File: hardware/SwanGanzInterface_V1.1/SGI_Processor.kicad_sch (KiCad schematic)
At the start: 29 parts, among them J2 Conn_01x08_Pin, SW2 MODE, SW3 ENTER, SW4 MODE, U4 XM0G3507QPTRQ1, U5 AdaFruit_1590, Y1 ABM8AIG-40.000MHZ-12-2Z-T3

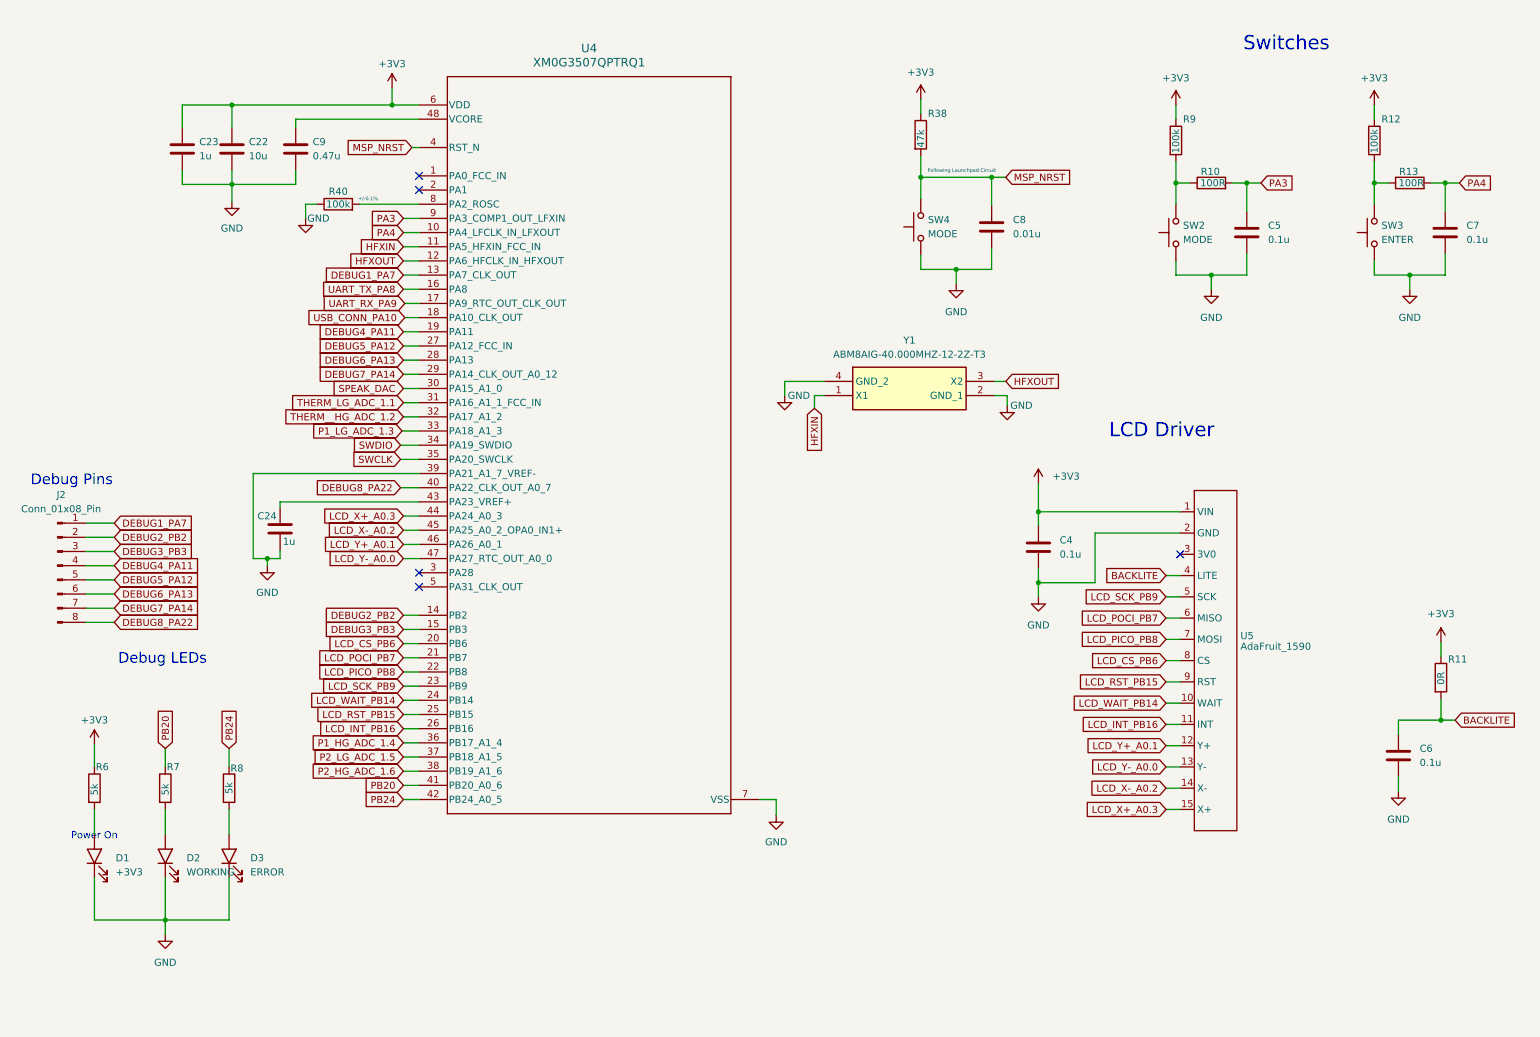
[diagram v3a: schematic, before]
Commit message: Worked on FT232R circuit - RTS, CTS etc
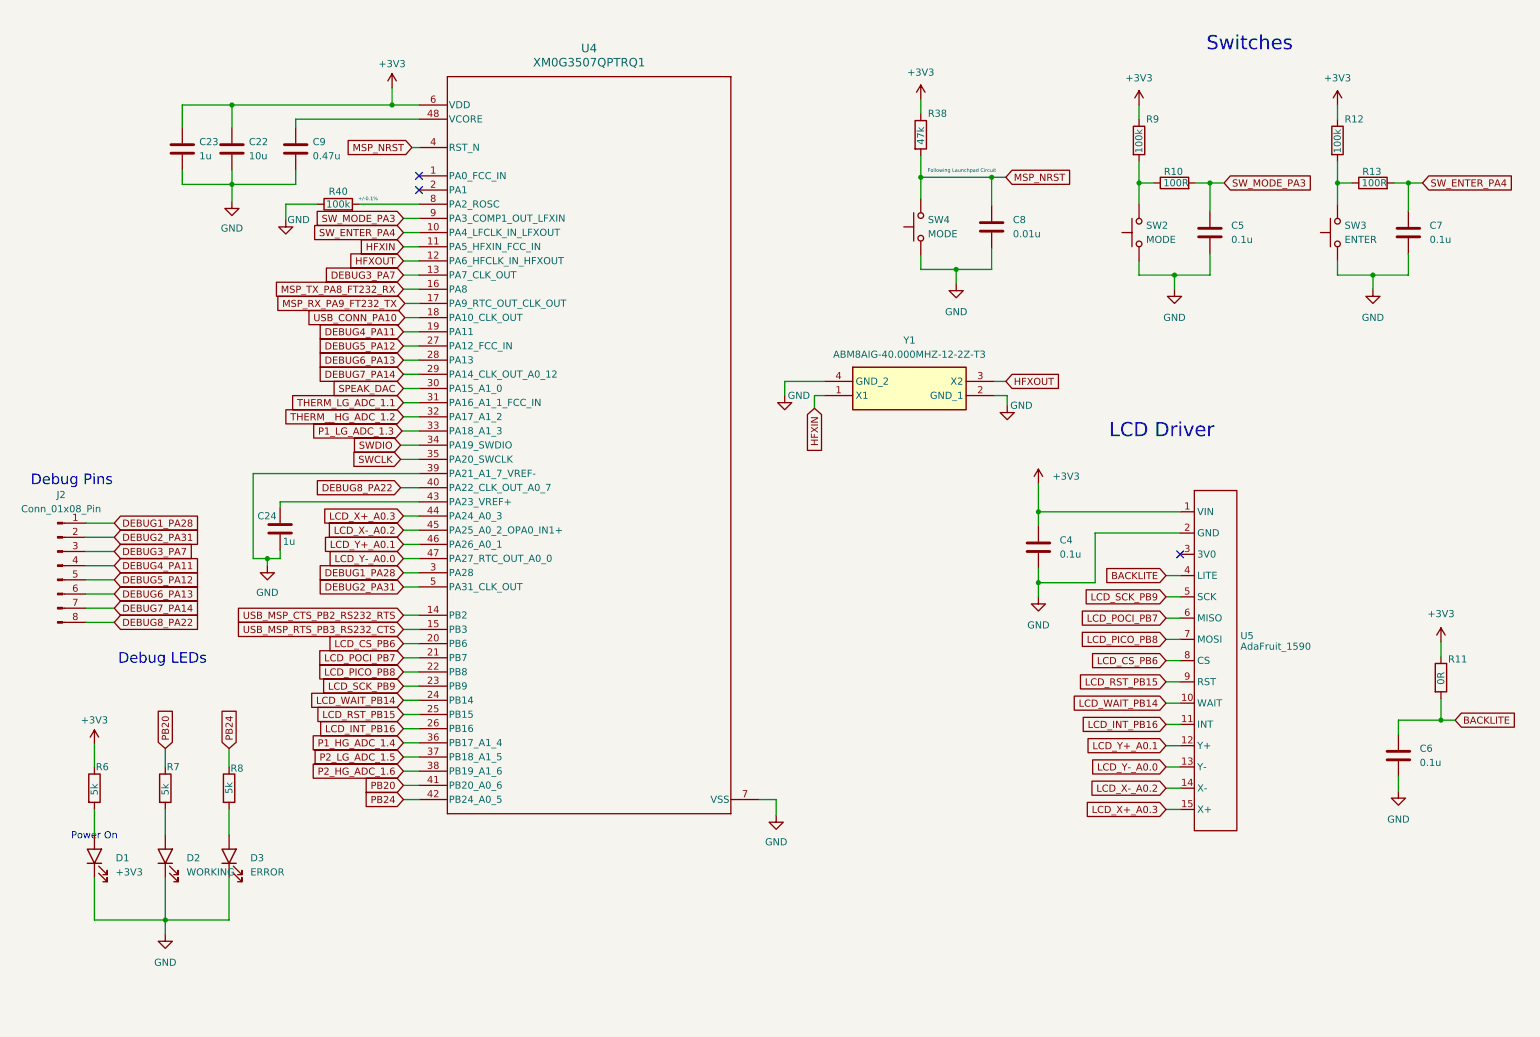
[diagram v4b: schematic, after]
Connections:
- net DEBUG1_PA28: now reaches U4.3 (PA28)
- net DEBUG1_PA28: now also J2.1 (Pin_1)
- net DEBUG2_PA31: now reaches U4.5 (PA31_CLK_OUT)
- net DEBUG2_PA31: now also J2.2 (Pin_2)
- net DEBUG1_PA7 renamed DEBUG3_PA7
- net DEBUG3_PA7: now also J2.3 (Pin_3); no longer J2.1 (Pin_1)
- net DEBUG2_PB2 renamed USB_MSP_CTS_PB2_RS232_RTS
- net USB_MSP_CTS_PB2_RS232_RTS: no longer J2.2 (Pin_2)
- net DEBUG3_PB3 renamed USB_MSP_RTS_PB3_RS232_CTS
- net USB_MSP_RTS_PB3_RS232_CTS: no longer J2.3 (Pin_3)
- net PA3 renamed SW_MODE_PA3
- net PA4 renamed SW_ENTER_PA4
- net UART_RX_PA9 renamed MSP_RX_PA9_FT232_TX
- net UART_TX_PA8 renamed MSP_TX_PA8_FT232_RX
- no-connect marks 5 -> 3
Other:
- moved on the sheet: C5, C7, R10, R12, R13, R9, SW2, SW3

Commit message: Added crystal loading caps
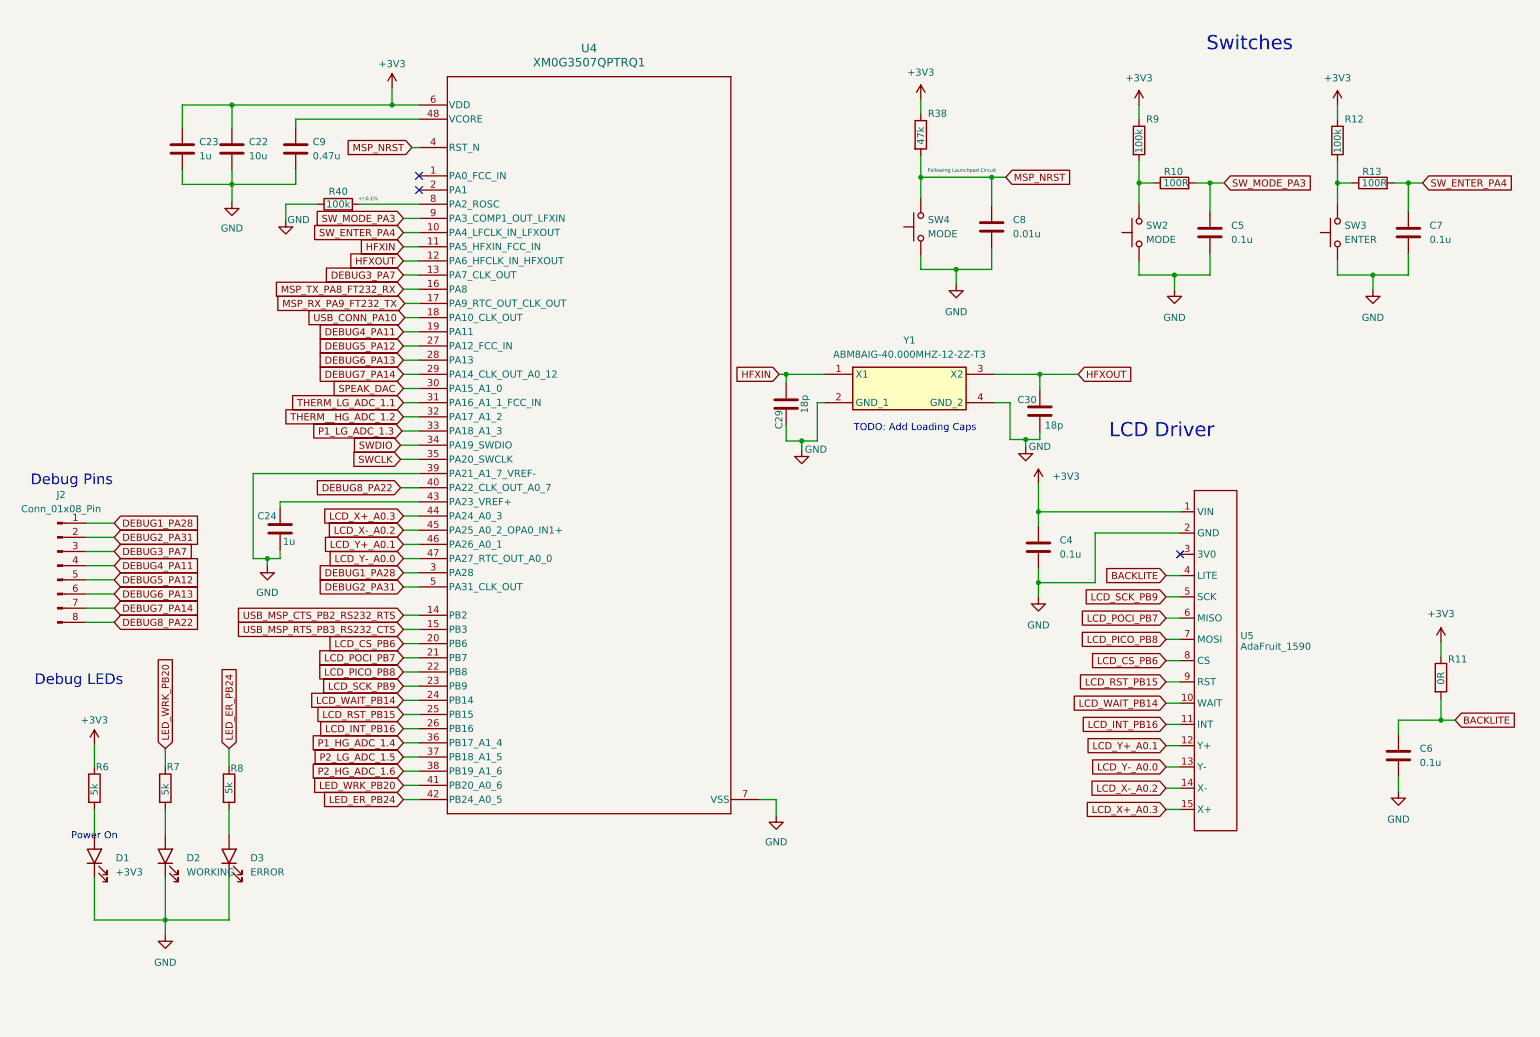
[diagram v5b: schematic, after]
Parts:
- added C29, C30: 18p, symbol Device:C
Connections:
- net GND: now also C29.1, C30.1
- net HFXIN: now also C29.2
- net HFXOUT: now also C30.2
- net PB20 renamed LED_WRK_PB20
- net PB24 renamed LED_ER_PB24
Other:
- note added: "TODO: Add Loading Caps"

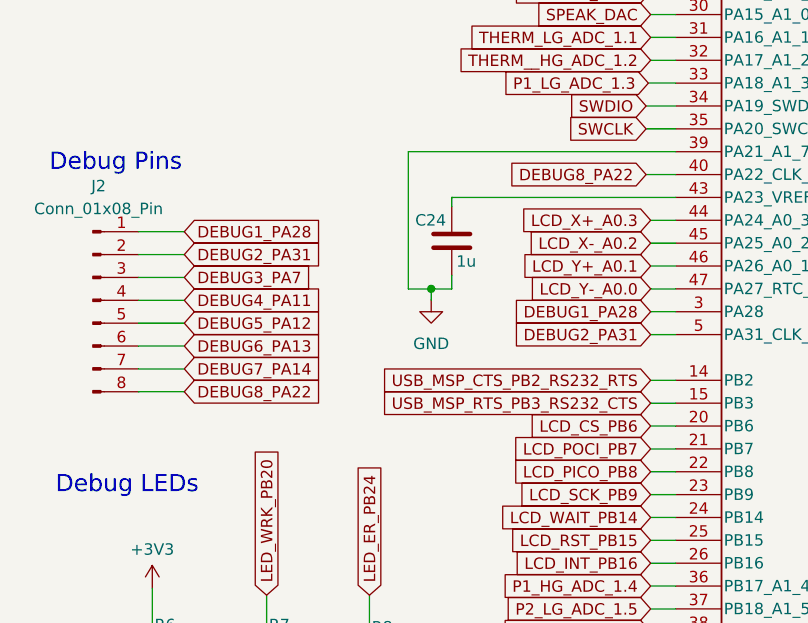
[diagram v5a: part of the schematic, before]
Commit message: Added work on FT232, added transmit and receieve leds
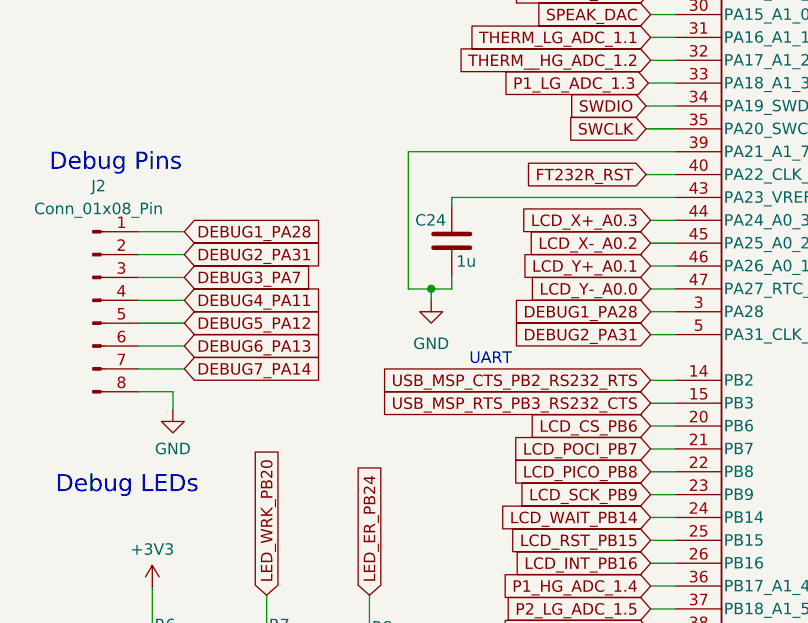
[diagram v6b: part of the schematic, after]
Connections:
- net GND: now also J2.8 (Pin_8)
- net DEBUG8_PA22 renamed FT232R_RST
- net FT232R_RST: no longer J2.8 (Pin_8)
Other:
- note added: "UART"
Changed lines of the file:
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@@
 		)
 	)
+	(text "UART"
+		(exclude_from_sim no)
+		(at 65.532 119.634 0)
+		(effects
+			(font
+				(size 1.27 1.27)
+			)
+		)
+	)
 	(text "Debug Pins"
 		(exclude_from_sim no)
@@
 	(wire
 		(pts
+			(xy 30.226 123.19) (xy 30.226 125.222)
+		)
+		(stroke
+			(width 0)
+			(type default)
+		)
+	)
+	(wire
+		(pts
 			(xy 26.416 113.03) (xy 31.496 113.03)
 		)
@@
 	(wire
 		(pts
+			(xy 26.416 123.19) (xy 30.226 123.19)
+		)
+		(stroke
+			(width 0)
+			(type default)
+		)
+	)
+	(wire
+		(pts
 			(xy 52.07 145.796) (xy 52.07 149.098)
 		)
@@
 	(wire
 		(pts
-			(xy 26.416 123.19) (xy 31.496 123.19)
-		)
-		(stroke
-			(width 0)
-			(type default)
-		)
-	)
-	(wire
-		(pts
 			(xy 197.104 118.618) (xy 197.104 116.078)
 		)
@@
 		)
 	)
-	(global_label "DEBUG8_PA22"
-		(shape input)
-		(at 31.496 123.19 0)
-		(fields_autoplaced yes)
-		(effects
-			(font
-				(size 1.27 1.27)
-			)
-			(justify left)
-		)
-		(property "Intersheetrefs" "${INTERSHEET_REFS}"
-			(at 47.7254 123.19 0)
-			(effects
-				(font
-					(size 1.27 1.27)
-				)
-				(justify left)
-				(hide yes)
-			)
-		)
-	)
 	(global_label "DEBUG2_PA31"
 		(shape input)
@@
 		)
 	)
-	(global_label "DEBUG8_PA22"
+	(global_label "FT232R_RST"
 		(shape input)
 		(at 82.804 99.06 180)
@@
 		)
 		(property "Intersheetrefs" "${INTERSHEET_REFS}"
-			(at 66.5746 99.06 0)
+			(at 68.4494 99.06 0)
 			(effects
 				(font
@@
 					(unit 1)
 				)
+			)
+		)
+	)
+	(symbol
+		(lib_id "power:GND")
+		(at 30.226 125.222 0)
+		(unit 1)
+		(exclude_from_sim no)
+		(in_bom yes)
+		(on_board yes)
+		(dnp no)
+		(fields_autoplaced yes)
+		(property "Reference" "#PWR084"
+			(at 30.226 131.572 0)
+			(effects
+				(font
+					(size 1.27 1.27)
+				)
+				(hide yes)
+			)
+		)
+		(property "Value" "GND"
+			(at 30.226 129.54 0)
+			(effects
+				(font
+					(size 1.27 1.27)
+				)
+			)
+		)
+		(property "Footprint" ""
+			(at 30.226 125.222 0)
+			(effects
+				(font
+					(size 1.27 1.27)
+				)
+				(hide yes)
+			)
+		)
+		(property "Datasheet" ""
+			(at 30.226 125.222 0)
+			(effects
+				(font
+					(size 1.27 1.27)
+				)
+				(hide yes)
+			)
+		)
+		(property "Description" "Power symbol creates a global label with name \"GND\" , ground"
+			(at 30.226 125.222 0)
+			(effects
+				(font
+					(size 1.27 1.27)
+				)
+				(hide yes)
+			)
+		)
+		(pin "1"
+		)
+		(instances
+			(project ""
+				(path "/4e9a6e30-f660-472b-9696-bea1f34b4545/b7986f9d-7bcd-462e-9f66-fb6deb5be406"
+					(reference "#PWR084")
+					(unit 1)
+				)
